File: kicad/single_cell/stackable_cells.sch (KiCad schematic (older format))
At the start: 11 parts, among them J1 cell_+, J2 cell_-, J3 bal_even_left, J4 bal_even_right, J5 bal_odd_left, J6 bal_odd_right

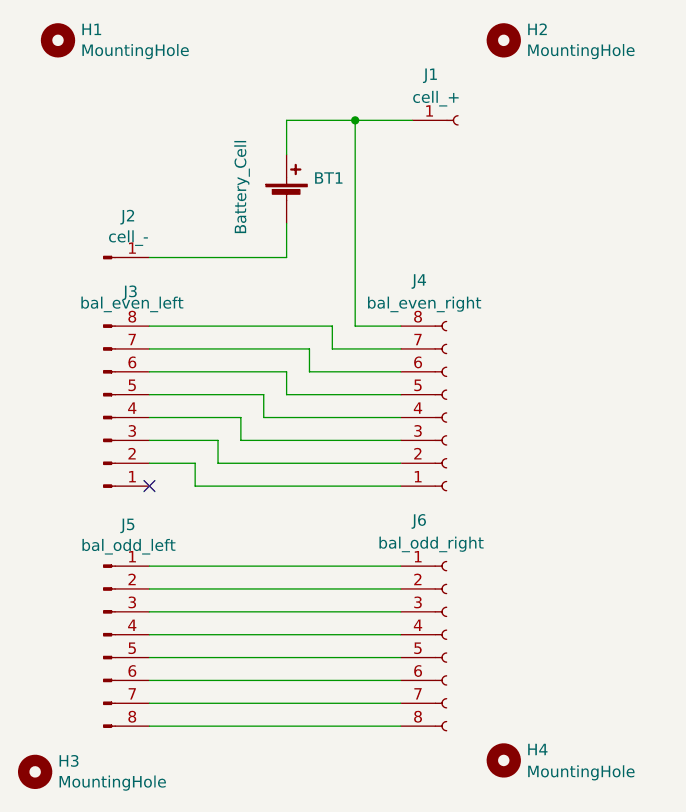
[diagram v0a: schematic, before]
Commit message: Finished four cells PCB
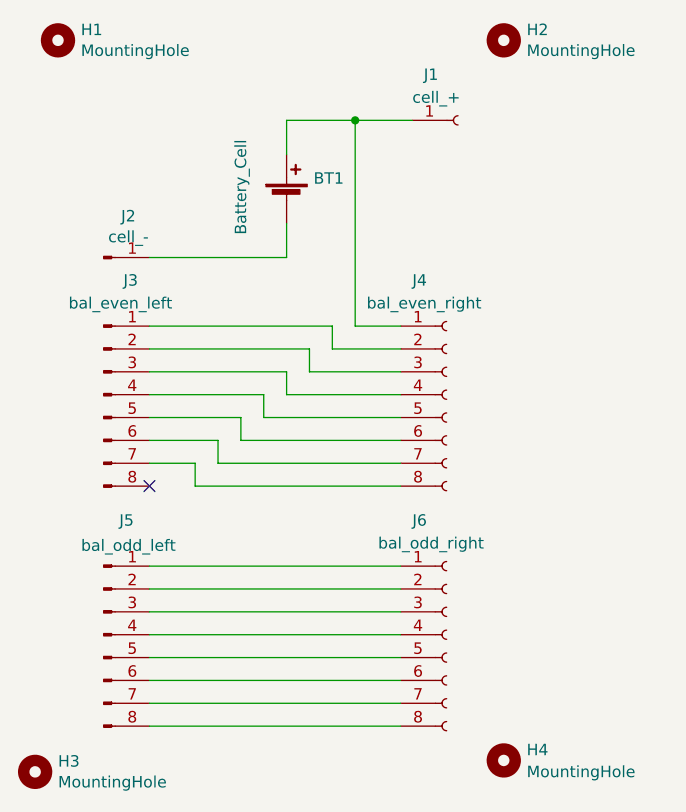
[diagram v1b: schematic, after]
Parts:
- J1: footprint Connector_PinSocket_2.54mm:PinSocket_1x01_P2.54mm_Horizontal -> telec:Castellated_1x01_P5.08mm
- J2: footprint Connector_PinHeader_2.54mm:PinHeader_1x01_P2.54mm_Horizontal -> telec:Castellated_1x01_P5.08mm
- J3, J5: footprint Connector_PinHeader_2.54mm:PinHeader_1x08_P2.54mm_Horizontal -> telec:Castellated_1x08_P2.54mm
- J4, J6: footprint Connector_PinSocket_2.54mm:PinSocket_1x08_P2.54mm_Horizontal -> telec:Castellated_1x08_P2.54mm
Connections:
- net at BT1.1 (+), J1.1 (Pin_1): now also J4.1 (Pin_1); no longer J4.8 (Pin_8)
- net at J3.2 (Pin_2): now also J4.3 (Pin_3); no longer J4.1 (Pin_1)
- net at J4.2 (Pin_2): now also J3.1 (Pin_1); no longer J3.3 (Pin_3)
- net at J3.4 (Pin_4): now also J4.5 (Pin_5); no longer J4.3 (Pin_3)
- net at J4.4 (Pin_4): now also J3.3 (Pin_3); no longer J3.5 (Pin_5)
- net at J3.6 (Pin_6): now also J4.7 (Pin_7); no longer J4.5 (Pin_5)
- net at J4.6 (Pin_6): now also J3.5 (Pin_5); no longer J3.7 (Pin_7)
- net at J3.8 (Pin_8): no longer J4.7 (Pin_7)
- new net: J3.7 (Pin_7), J4.8 (Pin_8)
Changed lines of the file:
@@
 L Connector:Conn_01x08_Female J4
 U 1 1 608868D9
-P 2800 2400
-F 0 "J4" H 2650 1800 50  0000 L CNN
-F 1 "bal_even_right" H 2450 1900 50  0000 L CNN
-F 2 "Connector_PinSocket_2.54mm:PinSocket_1x08_P2.54mm_Horizontal" H 2800 2400 50  0001 C CNN
-F 3 "~" H 2800 2400 50  0001 C CNN
-	1    2800 2400
-	1    0    0    1
+P 2800 2300
+F 0 "J4" H 2650 2800 50  0000 L CNN
+F 1 "bal_even_right" H 2450 2700 50  0000 L CNN
+F 2 "telec:Castellated_1x08_P2.54mm" H 2800 2300 50  0001 C CNN
+F 3 "~" H 2800 2300 50  0001 C CNN
+	1    2800 2300
+	1    0    0    -1
 $EndComp
 $Comp
@@
 F 0 "J6" H 2650 3850 50  0000 L CNN
 F 1 "bal_odd_right" H 2500 3750 50  0000 L CNN
-F 2 "Connector_PinSocket_2.54mm:PinSocket_1x08_P2.54mm_Horizontal" H 2800 3350 50  0001 C CNN
+F 2 "telec:Castellated_1x08_P2.54mm" H 2800 3350 50  0001 C CNN
 F 3 "~" H 2800 3350 50  0001 C CNN
 	1    2800 3350
@@
 U 1 1 608882E0
 P 1300 3350
-F 0 "J5" H 1408 3831 50  0000 C CNN
+F 0 "J5" H 1400 3850 50  0000 C CNN
 F 1 "bal_odd_left" H 1408 3740 50  0000 C CNN
-F 2 "Connector_PinHeader_2.54mm:PinHeader_1x08_P2.54mm_Horizontal" H 1300 3350 50  0001 C CNN
+F 2 "telec:Castellated_1x08_P2.54mm" H 1300 3350 50  0001 C CNN
 F 3 "~" H 1300 3350 50  0001 C CNN
 	1    1300 3350
@@
 F 0 "J1" H 2700 1300 50  0000 L CNN
 F 1 "cell_+" H 2650 1200 50  0000 L CNN
-F 2 "Connector_PinSocket_2.54mm:PinSocket_1x01_P2.54mm_Horizontal" H 2850 1100 50  0001 C CNN
+F 2 "telec:Castellated_1x01_P5.08mm" H 2850 1100 50  0001 C CNN
 F 3 "~" H 2850 1100 50  0001 C CNN
 	1    2850 1100
@@
 F 0 "J2" H 1408 1881 50  0000 C CNN
 F 1 "cell_-" H 1408 1790 50  0000 C CNN
-F 2 "Connector_PinHeader_2.54mm:PinHeader_1x01_P2.54mm_Horizontal" H 1300 1700 50  0001 C CNN
+F 2 "telec:Castellated_1x01_P5.08mm" H 1300 1700 50  0001 C CNN
 F 3 "~" H 1300 1700 50  0001 C CNN
 	1    1300 1700
@@
 L Connector:Conn_01x08_Male J3
 U 1 1 6088705C
-P 1300 2400
-F 0 "J3" H 1450 1850 50  0000 R CNN
-F 1 "bal_even_left" H 1650 1900 50  0000 R CNN
-F 2 "Connector_PinHeader_2.54mm:PinHeader_1x08_P2.54mm_Horizontal" H 1300 2400 50  0001 C CNN
-F 3 "~" H 1300 2400 50  0001 C CNN
-	1    1300 2400
-	1    0    0    1
+P 1300 2300
+F 0 "J3" H 1450 2800 50  0000 R CNN
+F 1 "bal_even_left" H 1600 2700 50  0000 R CNN
+F 2 "telec:Castellated_1x08_P2.54mm" H 1300 2300 50  0001 C CNN
+F 3 "~" H 1300 2300 50  0001 C CNN
+	1    1300 2300
+	1    0    0    -1
 $EndComp
 Wire Wire Line
